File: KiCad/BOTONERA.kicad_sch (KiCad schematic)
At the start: 8 parts, among them SW1 SW_Push, SW2 SW_Push, SW3 SW_Push, SW4 SW_Push

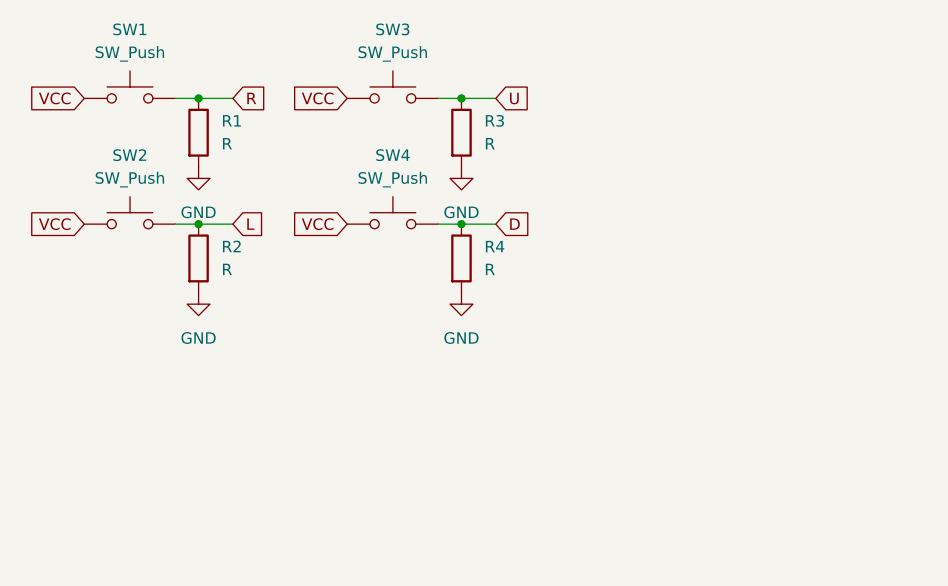
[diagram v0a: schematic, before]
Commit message: añadido retrovisor izquierdo
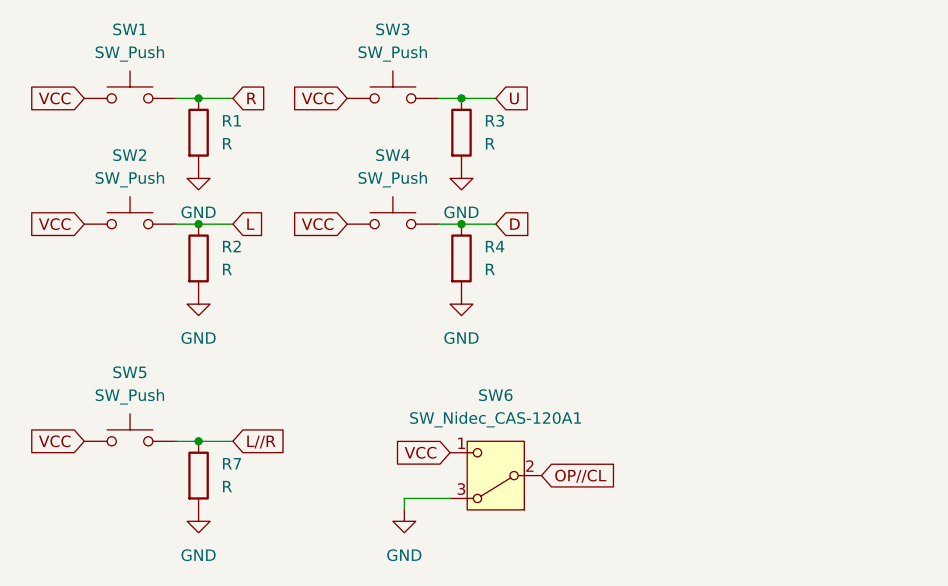
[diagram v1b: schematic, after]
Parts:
- added R7: R, symbol Device:R
- added SW5: SW_Push, symbol Switch:SW_Push
- added SW6: SW_Nidec_CAS-120A1, Button_Switch_SMD:Nidec_Copal_CAS-120A, symbol Switch:SW_Nidec_CAS-120A1
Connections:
- net GND: now also R7.2, SW6.3 (A)
- net VCC: now also SW5.1, SW6.1 (C)
- new net L//R: R7.1, SW5.2
- new net OP//CL: SW6.2 (B)

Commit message: reducido motores y finales de carrera
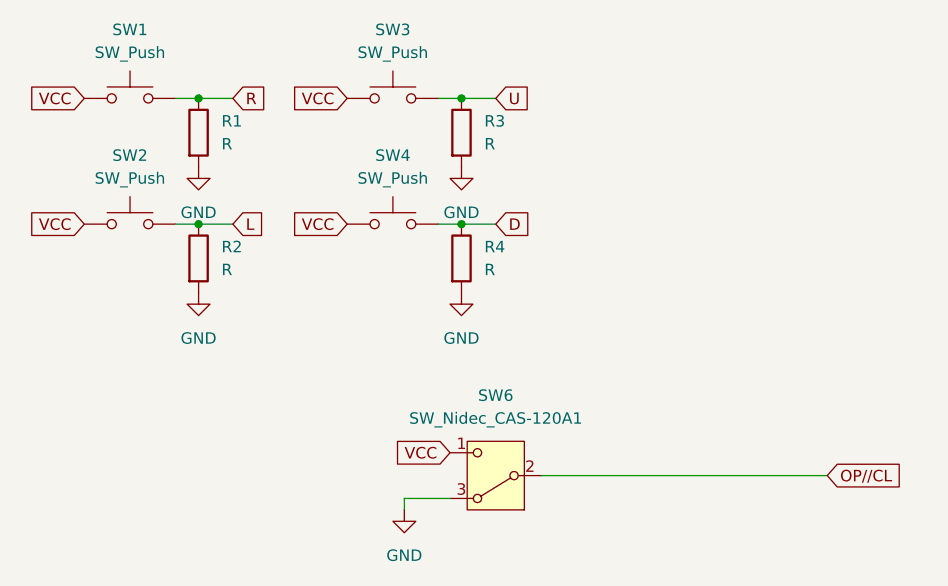
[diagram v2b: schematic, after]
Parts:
- removed R7: R, symbol Device:R
- removed SW5: SW_Push, symbol Switch:SW_Push

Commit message: he añadido huelas a algunos componentes importates
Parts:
- SW1, SW2, SW3, SW4: footprint (none) -> Button_Switch_SMD:SW_Push_1P1T_NO_E-Switch_TL3301NxxxxxG
- SW6: footprint Button_Switch_SMD:Nidec_Copal_CAS-120A -> Button_Switch_SMD:SW_DIP_SPSTx01_Slide_9.78x4.72mm_W8.61mm_P2.54mm
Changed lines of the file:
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@@
 			)
 		)
-		(property "Footprint" ""
+		(property "Footprint" "Button_Switch_SMD:SW_Push_1P1T_NO_E-Switch_TL3301NxxxxxG"
 			(at 158.75 96.52 0)
 			(effects
@@
 			)
 		)
-		(property "Footprint" ""
+		(property "Footprint" "Button_Switch_SMD:SW_Push_1P1T_NO_E-Switch_TL3301NxxxxxG"
 			(at 158.75 82.55 0)
 			(effects
@@
 			)
 		)
-		(property "Footprint" "Button_Switch_SMD:Nidec_Copal_CAS-120A"
+		(property "Footprint" "Button_Switch_SMD:SW_DIP_SPSTx01_Slide_9.78x4.72mm_W8.61mm_P2.54mm"
 			(at 170.18 119.38 0)
 			(effects
@@
 			)
 		)
-		(property "Footprint" ""
+		(property "Footprint" "Button_Switch_SMD:SW_Push_1P1T_NO_E-Switch_TL3301NxxxxxG"
 			(at 129.54 96.52 0)
 			(effects
@@
 			)
 		)
-		(property "Footprint" ""
+		(property "Footprint" "Button_Switch_SMD:SW_Push_1P1T_NO_E-Switch_TL3301NxxxxxG"
 			(at 129.54 82.55 0)
 			(effects

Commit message: he añadido el resto de huellas, he corregido algunos errores en la parte de alimentación en los diodos. tambien he trasladados todas las huellas a la pcb y lo he intentado separar un poco para verlo mas claro cuando empecemos el placing.
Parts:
- R1, R2, R3, R4: footprint (none) -> Resistor_SMD:R_0402_1005Metric
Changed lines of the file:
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@@
 			)
 		)
-		(property "Footprint" ""
+		(property "Footprint" "Resistor_SMD:R_0402_1005Metric"
 			(at 164.592 105.41 90)
 			(effects
@@
 			)
 		)
-		(property "Footprint" ""
+		(property "Footprint" "Resistor_SMD:R_0402_1005Metric"
 			(at 135.382 105.41 90)
 			(effects
@@
 			)
 		)
-		(property "Footprint" ""
+		(property "Footprint" "Resistor_SMD:R_0402_1005Metric"
 			(at 135.382 91.44 90)
 			(effects
@@
 			)
 		)
-		(property "Footprint" ""
+		(property "Footprint" "Resistor_SMD:R_0402_1005Metric"
 			(at 164.592 91.44 90)
 			(effects
